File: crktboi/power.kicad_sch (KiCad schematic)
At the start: 17 parts, among them U2 4700uF, U3 4700uF, U4 BQ25505RGRT

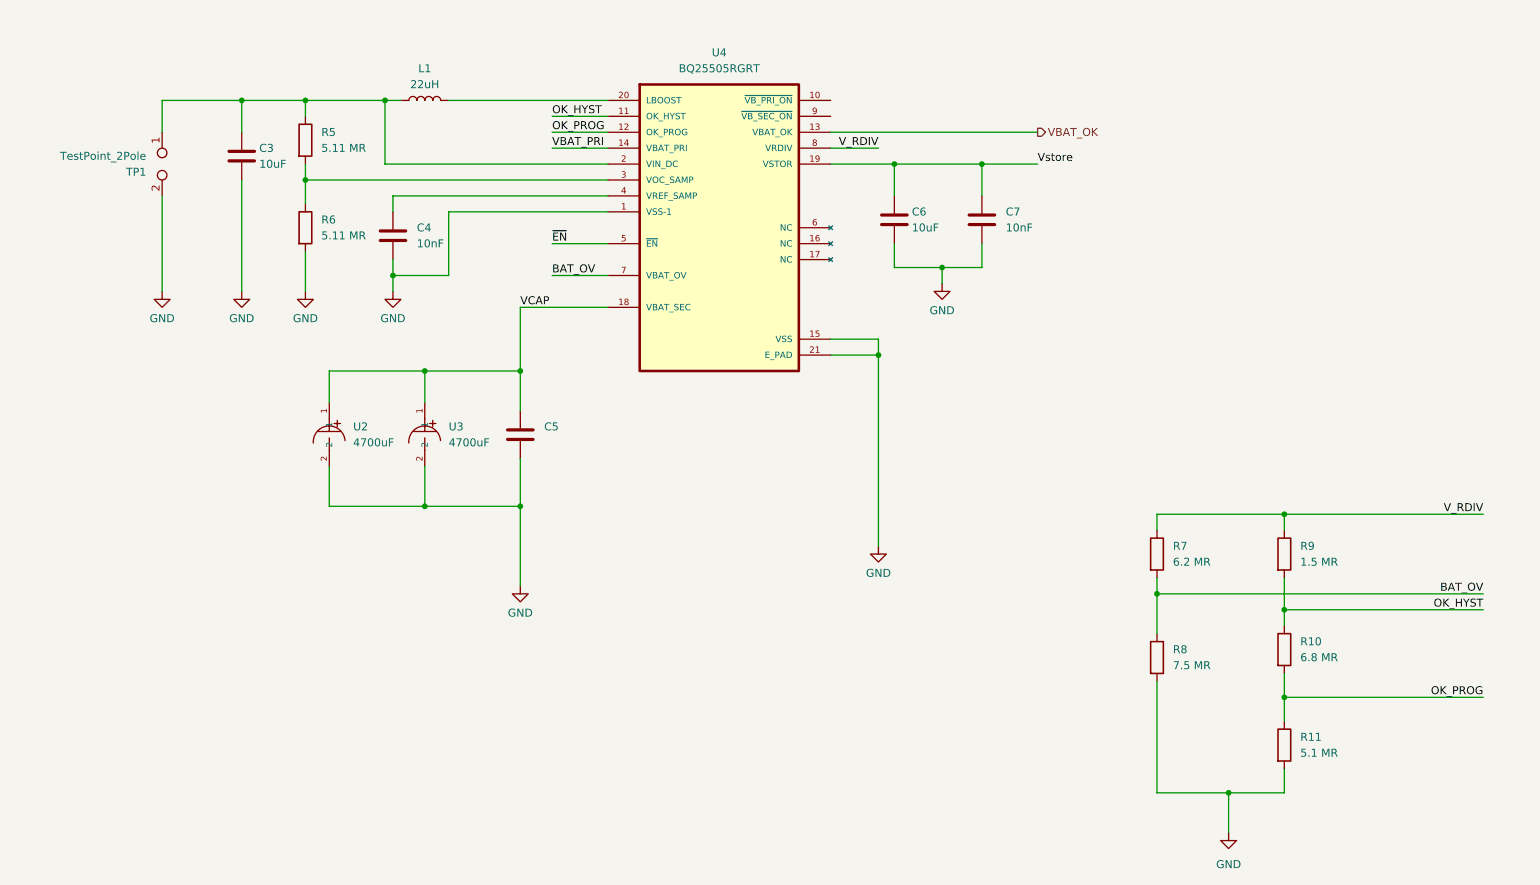
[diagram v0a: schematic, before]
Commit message: Added a plan document & updated  design with tweaks for 3S3P photodiodes
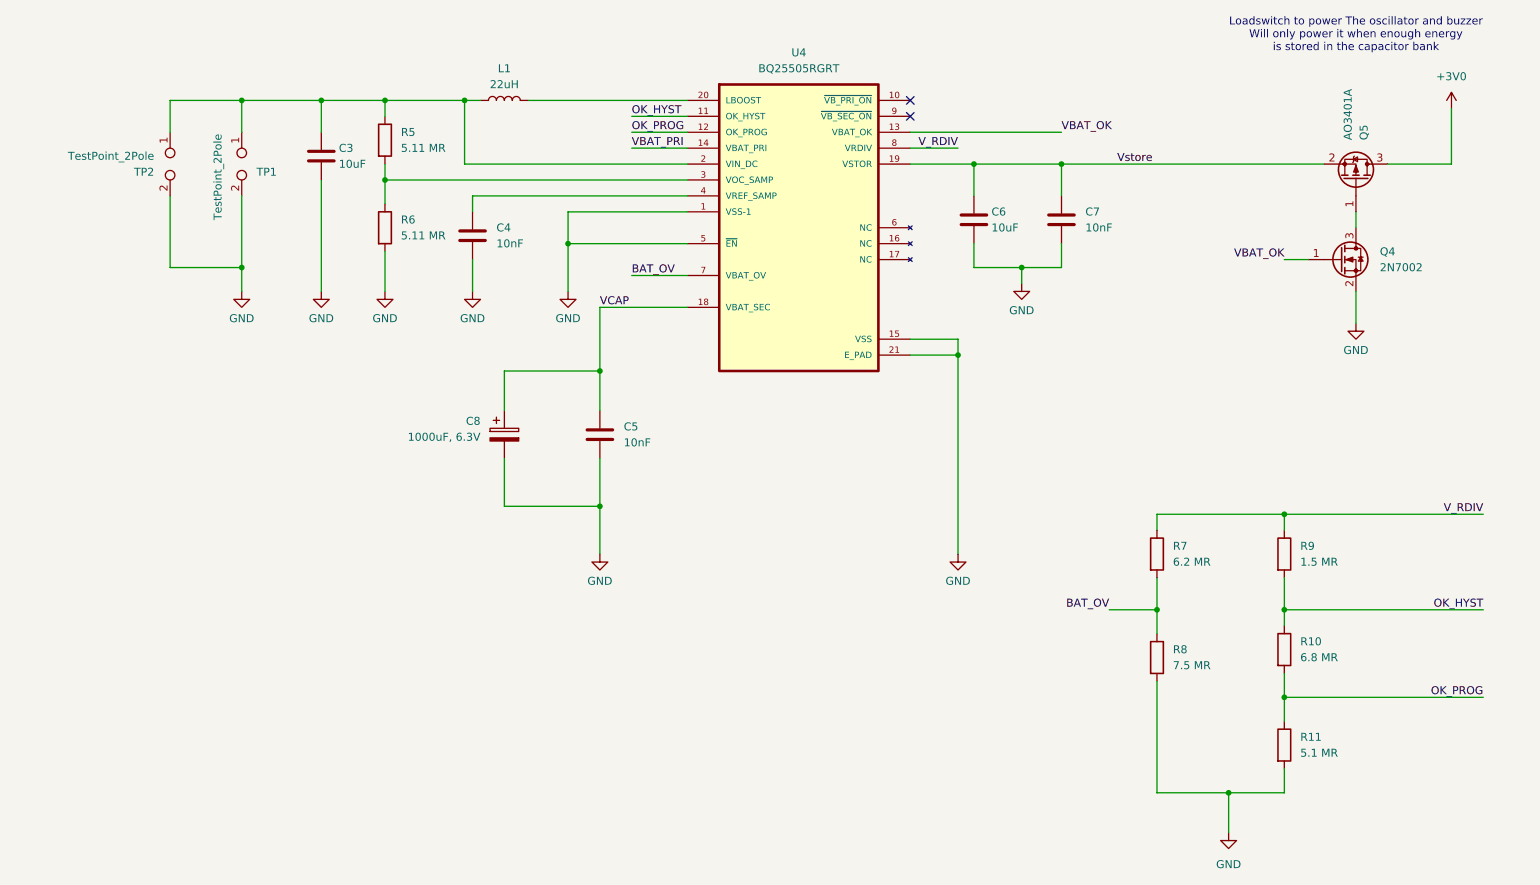
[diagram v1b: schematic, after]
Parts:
- removed U2, U3: 4700uF, HS0J478M1016PC:CAP-TH_BD10.0-F5.00-D0.6-FD, symbol HS0J478M1016PC:HS0J478M1016PC
- added C8: 1000uF, 6.3V, Capacitor_SMD:CP_Elec_8x10, symbol Device:C_Polarized
- added Q4: 2N7002, Package_TO_SOT_SMD:SOT-23, symbol Transistor_FET:2N7002
- added Q5: AO3401A, Package_TO_SOT_SMD:SOT-23, symbol Transistor_FET:AO3401A
- added TP2: TestPoint_2Pole, Connector_PinSocket_2.54mm:PinSocket_2x01_P2.54mm_Vertical, symbol Connector:TestPoint_2Pole
- C5: LCSC (none) -> C327025
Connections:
- net ~{EN} is gone; now on net GND: U4.5 (~{EN})
- net GND: now also C8.2, Q4.2 (S), TP2.2
- net VBAT_OK: now also Q4.1 (G)
- net VCAP: now also C8.1
- net Vstore: now also Q5.2 (S)
- net at C3.1, L1.1, R5.1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: now also TP2.1
- new net: Q4.3 (D), Q5.1 (G)
- new net +3V0: Q5.3 (D)
- no-connect marks 0 -> 2
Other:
- note added: "Loadswitch to power The oscillator and buzzer Will only power it when enough energy is stored in the capacitor bank"
- moved on the sheet: C3, C4, C6, C7, L1, R5, R6, TP1, U4

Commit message: Added LCSC part numbers to each part in the schematic
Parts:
- C3, C6: LCSC (none) -> C307520
- C4, C7: LCSC (none) -> C327025
- L1: LCSC (none) -> C383411
- Q5: LCSC (none) -> C15127
- R10: LCSC (none) -> C477775
- R11: LCSC (none) -> C477747
- R5, R6: LCSC (none) -> C477744
- R7: LCSC (none) -> C477768
- R8: LCSC (none) -> C327241
- R9: LCSC (none) -> C138034
- TP1, TP2: LCSC (none) -> C492401
- U4: LCSC (none) -> C2876730
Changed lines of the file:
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@@
 			)
 		)
+		(property "LCSC" "C327025"
+			(at 179.07 55.88 0)
+			(hide yes)
+			(show_name no)
+			(do_not_autoplace no)
+			(effects
+				(font
+					(size 1.27 1.27)
+				)
+			)
+		)
 		(pin "1"
 		)
@@
 			)
 		)
+		(property "LCSC" "C383411"
+			(at 90.17 36.83 0)
+			(hide yes)
+			(show_name no)
+			(do_not_autoplace no)
+			(effects
+				(font
+					(size 1.27 1.27)
+				)
+			)
+		)
 		(pin "2"
 		)
@@
 			)
 		)
+		(property "LCSC" "C492401"
+			(at 48.26 46.99 0)
+			(hide yes)
+			(show_name no)
+			(do_not_autoplace no)
+			(effects
+				(font
+					(size 1.27 1.27)
+				)
+			)
+		)
 		(pin "1"
 		)
@@
 			)
 		)
+		(property "LCSC" "C327241"
+			(at 194.31 125.73 0)
+			(hide yes)
+			(show_name no)
+			(do_not_autoplace no)
+			(effects
+				(font
+					(size 1.27 1.27)
+				)
+			)
+		)
 		(pin "1"
 		)
@@
 			)
 		)
+		(property "LCSC" "C138034"
+			(at 214.63 109.22 0)
+			(hide yes)
+			(show_name no)
+			(do_not_autoplace no)
+			(effects
+				(font
+					(size 1.27 1.27)
+				)
+			)
+		)
 		(pin "1"
 		)
@@
 			)
 		)
+		(property "LCSC" "C477768"
+			(at 194.31 109.22 0)
+			(hide yes)
+			(show_name no)
+			(do_not_autoplace no)
+			(effects
+				(font
+					(size 1.27 1.27)
+				)
+			)
+		)
 		(pin "1"
 		)
@@
 			)
 		)
+		(property "LCSC" "C477747"
+			(at 214.63 139.7 0)
+			(hide yes)
+			(show_name no)
+			(do_not_autoplace no)
+			(effects
+				(font
+					(size 1.27 1.27)
+				)
+			)
+		)
 		(pin "1"
 		)
@@
 			)
 		)
+		(property "LCSC" "C477744"
+			(at 71.12 57.15 0)
+			(hide yes)
+			(show_name no)
+			(do_not_autoplace no)
+			(effects
+				(font
+					(size 1.27 1.27)
+				)
+			)
+		)
 		(pin "1"
 		)
@@
 			)
 		)
+		(property "LCSC" "C477744"
+			(at 71.12 43.18 0)
+			(hide yes)
+			(show_name no)
+			(do_not_autoplace no)
+			(effects
+				(font
+					(size 1.27 1.27)
+				)
+			)
+		)
 		(pin "1"
 		)
@@
 			)
 		)
+		(property "LCSC" "C307520"
+			(at 165.1 55.88 0)
+			(hide yes)
+			(show_name no)
+			(do_not_autoplace no)
+			(effects
+				(font
+					(size 1.27 1.27)
+				)
+			)
+		)
 		(pin "1"
 		)
@@
 			)
 		)
+		(property "LCSC" "C2876730"
+			(at 137.16 57.15 0)
+			(hide yes)
+			(show_name no)
+			(do_not_autoplace no)
+			(effects
+				(font
+					(size 1.27 1.27)
+				)
+			)
+		)
 		(pin "2"
 		)
@@
 			)
 		)
+		(property "LCSC" "C327025"
+			(at 85.09 58.42 0)
+			(hide yes)
+			(show_name no)
+			(do_not_autoplace no)
+			(effects
+				(font
+					(size 1.27 1.27)
+				)
+			)
+		)
 		(pin "1"
 		)
@@
 			)
 		)
+		(property "LCSC" "C492401"
+			(at 36.83 46.99 0)
+			(hide yes)
+			(show_name no)
+			(do_not_autoplace no)
+			(effects
+				(font
+					(size 1.27 1.27)
+				)
+			)
+		)
 		(pin "1"
 		)
@@
 			)
 		)
+		(property "LCSC" "C307520"
+			(at 60.96 45.72 0)
+			(hide yes)
+			(show_name no)
+			(do_not_autoplace no)
+			(effects
+				(font
+					(size 1.27 1.27)
+				)
+			)
+		)
 		(pin "1"
 		)
@@
 			)
 		)
+		(property "LCSC" "C477775"
+			(at 214.63 124.46 0)
+			(hide yes)
+			(show_name no)
+			(do_not_autoplace no)
+			(effects
+				(font
+					(size 1.27 1.27)
+				)
+			)
+		)
 		(pin "1"
 		)
@@
 			(at 226.06 49.53 0)
 			(hide yes)
+			(show_name no)
+			(do_not_autoplace no)
+			(effects
+				(font
+					(size 1.27 1.27)
+				)
+			)
+		)
+		(property "LCSC" "C15127"
+			(at 226.06 49.53 0)
+			(hide yes)

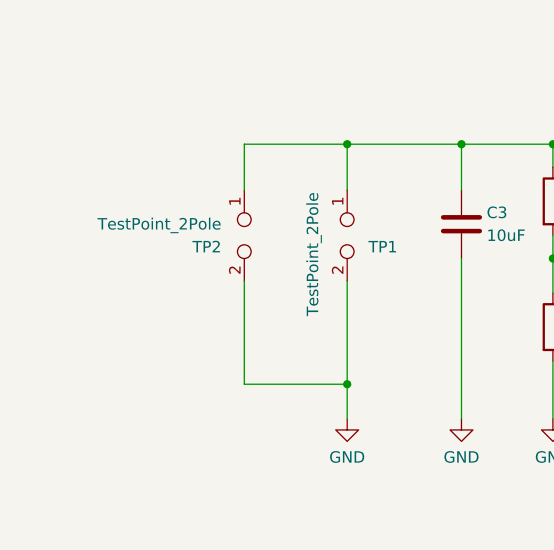
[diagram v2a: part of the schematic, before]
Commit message: Added photodiodes to the base design for eyes on the cicada.
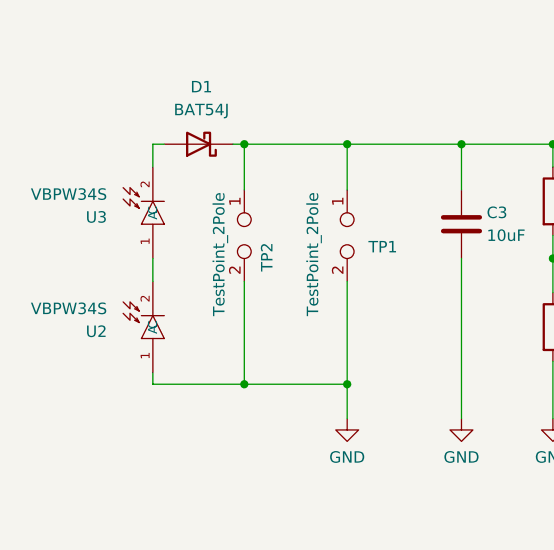
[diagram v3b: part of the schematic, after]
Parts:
- added D1: BAT54J, Diode_SMD:D_SOD-323F, symbol Diode:BAT54J
- added U2, U3: VBPW34S, VBPW34S:SENSOR-SMD_L4.4-W3.9, symbol VBPW34S:VBPW34S
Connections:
- net GND: now also U2.1 (A)
- net at C3.1, L1.1, R5.1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: now also D1.1 (K)
- new net: U2.2 (C), U3.1 (A)
- new net: D1.2 (A), U3.2 (C)

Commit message: Added resistors as legs for the cicada and updated LCSC part numbers for new parts
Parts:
- D1: LCSC (none) -> C130415
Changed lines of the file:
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@@
+			)
+		)
+		(property "LCSC" "C130415"
+			(at 31.75 36.83 0)
+			(hide yes)
+			(show_name no)
+			(do_not_autoplace no)
+			(effects
+				(font
+					(size 1.27 1.27)
+				)
 			)
 		)

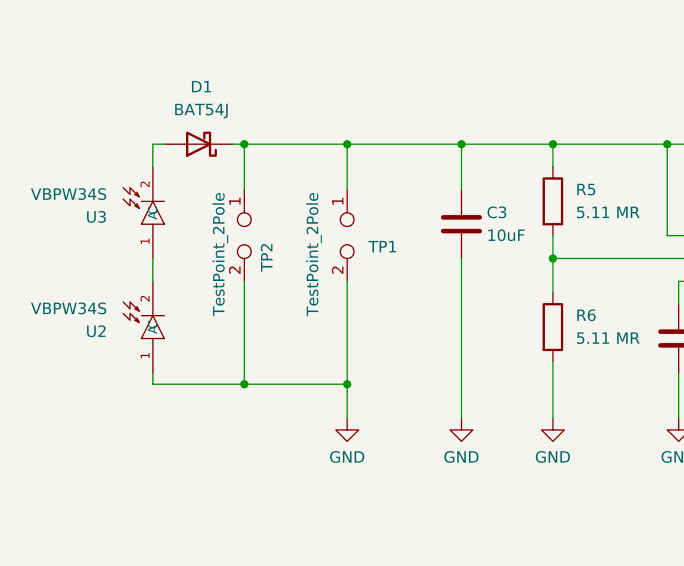
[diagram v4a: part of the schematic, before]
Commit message: Added BAT54J diodes to the input connectors of the PV headers
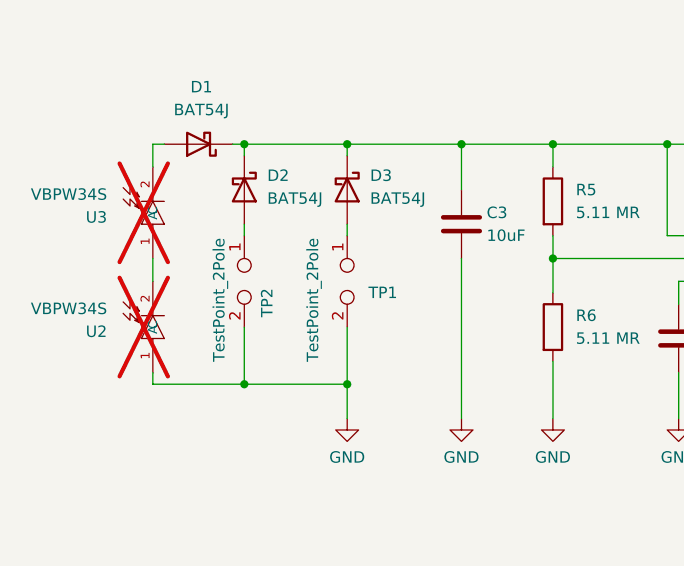
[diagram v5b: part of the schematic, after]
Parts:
- added D2, D3: BAT54J, Diode_SMD:D_SOD-323F, symbol Diode:BAT54J
- U2, U3: now not fitted
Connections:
- net at C3.1, D1.1 (K), L1.1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: now also D2.1 (K), D3.1 (K); no longer TP1.1, TP2.1
- new net: D3.2 (A), TP1.1
- new net: D2.2 (A), TP2.1
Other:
- moved on the sheet: TP1, TP2
